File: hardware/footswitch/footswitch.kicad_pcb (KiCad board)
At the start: 2 copper layers, 34 x 24 mm, 4 parts, among them J1 Conn_02x05_Counter_Clockwise

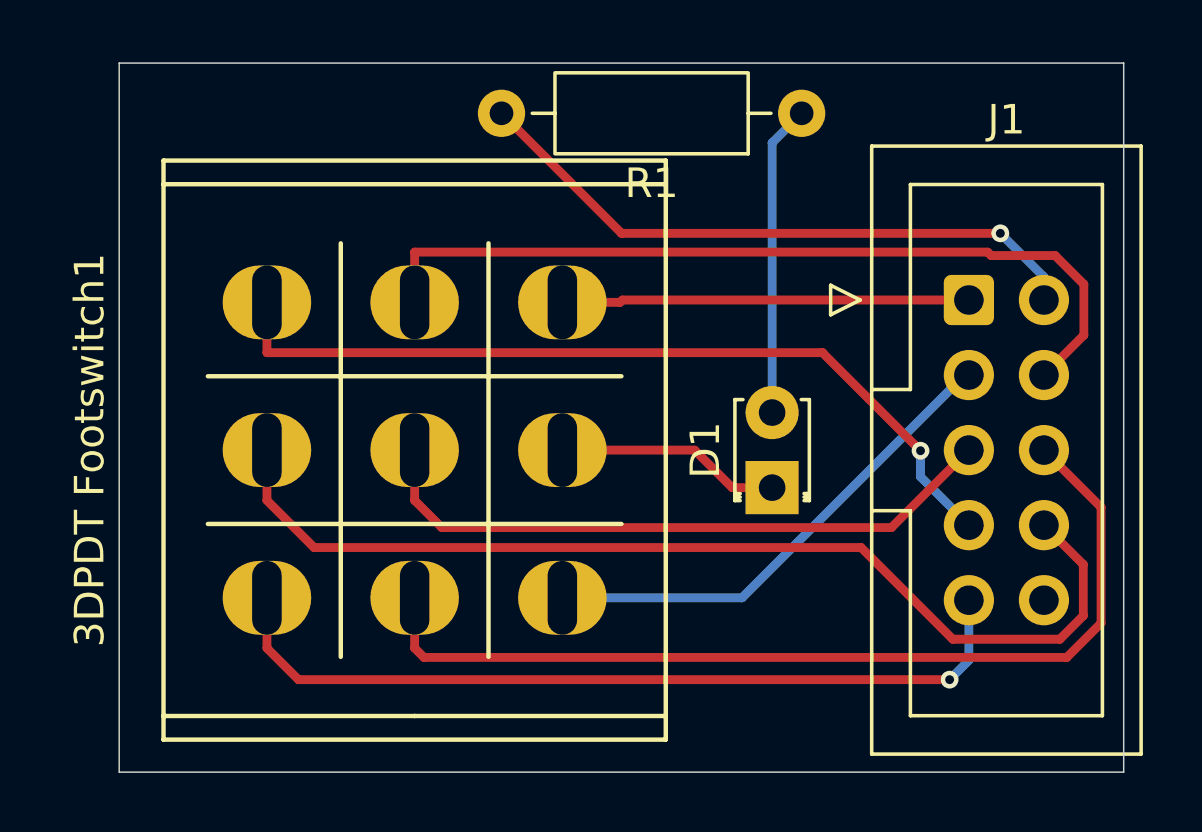
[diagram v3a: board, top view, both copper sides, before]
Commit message: Minor adjustments to footswitch pcb
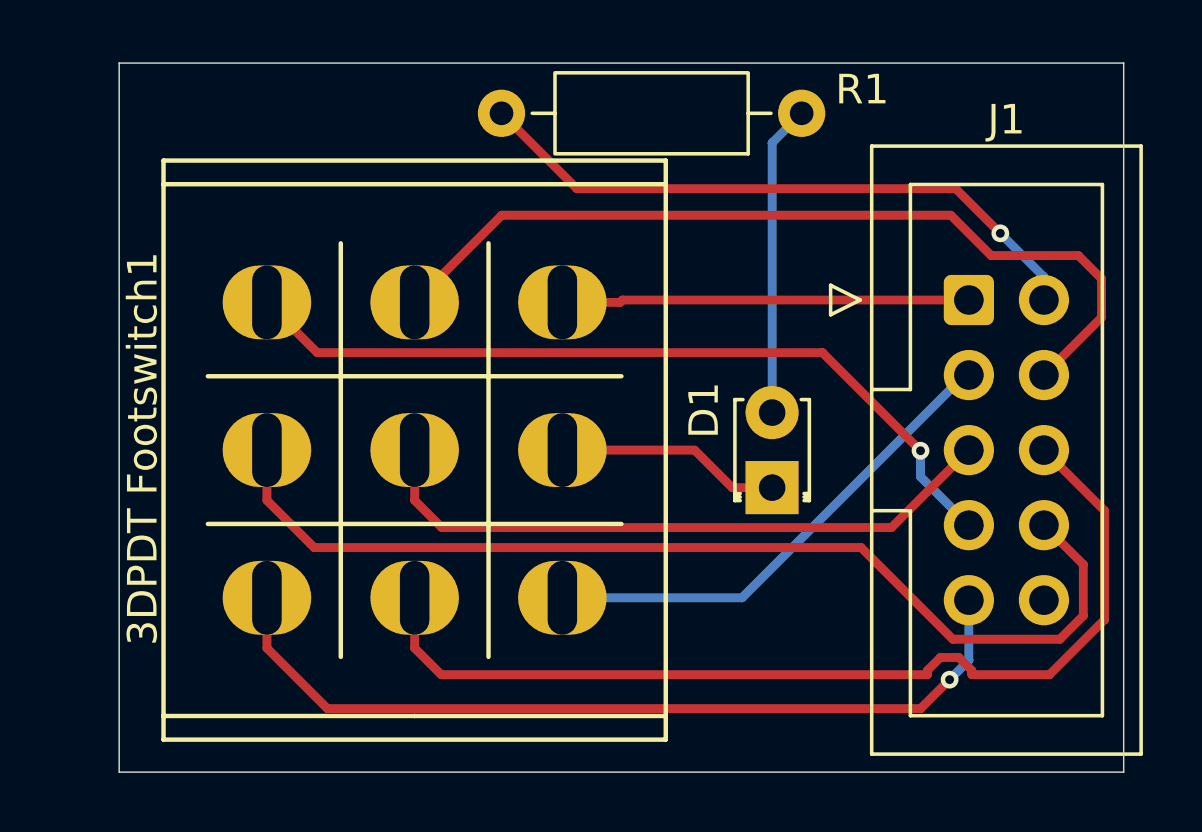
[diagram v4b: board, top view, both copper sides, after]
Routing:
- net /conn6: track 32.2 -> 33.4 mm
- net /conn7: track 28.4 -> 27.4 mm
- net /conn4: track 28.4 -> 29.4 mm
- net /conn9: track 28.2 -> 29.0 mm
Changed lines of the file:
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@@
 		(tags "Resistor Axial_DIN0207 series Axial Horizontal pin pitch 10.16mm 0.25W = 1/4W length 6.3mm diameter 2.5mm")
 		(property "Reference" "R1"
-			(at 5.08 -2.37 0)
+			(at -2.05 0.8 0)
 			(layer "F.SilkS")
 			(effects
@@
 		(tags "LED")
 		(property "Reference" "D1"
-			(at 1.27 -2.26 90)
+			(at 2.62 -2.3 90)
 			(layer "F.SilkS")
 			(effects
@@
 		(at 140 112.1 -90)
 		(property "Reference" "3DPDT Footswitch1"
-			(at 0 11 90)
+			(at -0.05 9.2 90)
 			(layer "F.SilkS")
 			(effects
@@
 	)
 	(segment
-		(start 135 117.1)
+		(start 135 118.8017)
+		(end 135 117.1)
+		(width 0.3)
+		(layer "F.Cu")
+		(net 2)
+	)
+	(segment
+		(start 158.1078 119.8694)
+		(end 157.1272 120.85)
+		(width 0.3)
+		(layer "F.Cu")
+		(net 2)
+	)
+	(segment
+		(start 137.0483 120.85)
 		(end 135 118.8017)
 		(width 0.3)
@@
 	)
 	(segment
-		(start 158.1078 119.8694)
-		(end 136.0677 119.8694)
-		(width 0.3)
-		(layer "F.Cu")
-		(net 2)
-	)
-	(segment
-		(start 136.0677 119.8694)
-		(end 135 118.8017)
+		(start 157.1272 120.85)
+		(end 137.0483 120.85)
 		(width 0.3)
 		(layer "F.Cu")
@@
 	)
 	(segment
-		(start 162.6515 106.4861)
-		(end 162.6515 108.2085)
+		(start 163.25 107.61)
+		(end 161.3 109.56)
 		(width 0.3)
 		(layer "F.Cu")
@@
 	)
 	(segment
-		(start 161.6801 105.5147)
-		(end 162.6515 106.4861)
+		(start 140 107.1)
+		(end 142.95 104.15)
 		(width 0.3)
 		(layer "F.Cu")
@@
 	(segment
 		(start 159.5137 105.5147)
-		(end 161.6801 105.5147)
+		(end 162.4647 105.5147)
 		(width 0.3)
 		(layer "F.Cu")
@@
 	)
 	(segment
-		(start 140 105.3983)
-		(end 159.3973 105.3983)
+		(start 163.25 106.3)
+		(end 163.25 107.61)
 		(width 0.3)
 		(layer "F.Cu")
@@
 	)
 	(segment
-		(start 162.6515 108.2085)
-		(end 161.3 109.56)
+		(start 162.4647 105.5147)
+		(end 163.25 106.3)
 		(width 0.3)
 		(layer "F.Cu")
@@
 	)
 	(segment
-		(start 140 107.1)
-		(end 140 105.3983)
+		(start 158.149 104.15)
+		(end 159.5137 105.5147)
 		(width 0.3)
 		(layer "F.Cu")
@@
 	)
 	(segment
-		(start 159.3973 105.3983)
-		(end 159.5137 105.5147)
+		(start 142.95 104.15)
+		(end 158.149 104.15)
 		(width 0.3)
 		(layer "F.Cu")
@@
 	)
 	(segment
-		(start 147.003 104.763)
+		(start 158.312 103.25)
+		(end 145.49 103.25)
+		(width 0.3)
+		(layer "F.Cu")
+		(net 4)
+	)
+	(segment
+		(start 145.49 103.25)
 		(end 142.94 100.7)
 		(width 0.3)
@@
 	(segment
 		(start 159.825 104.763)
-		(end 147.003 104.763)
+		(end 158.312 103.25)
 		(width 0.3)
 		(layer "F.Cu")
@@
 	)
 	(segment
+		(start 136.7017 108.8017)
+		(end 135 107.1)
+		(width 0.3)
+		(layer "F.Cu")
+		(net 5)
+	)
+	(segment
 		(start 153.8044 108.8017)
-		(end 135 108.8017)
+		(end 157.1234 112.1207)
 		(width 0.3)
 		(layer "F.Cu")
@@
 	)
 	(segment
-		(start 135 107.1)
-		(end 135 108.8017)
-		(width 0.3)
-		(layer "F.Cu")
-		(net 5)
-	)
-	(segment
-		(start 157.1234 112.1207)
-		(end 153.8044 108.8017)
+		(start 153.8044 108.8017)
+		(end 136.7017 108.8017)
 		(width 0.3)
 		(layer "F.Cu")
@@
 	)
 	(segment
-		(start 163.2344 117.9567)
-		(end 162.0734 119.1177)
+		(start 161.3 112.1)
+		(end 163.349 114.149)
 		(width 0.3)
 		(layer "F.Cu")
@@
 	)
 	(segment
-		(start 140 117.1)
+		(start 157.796725 119.1184)
+		(end 157.3568 119.558325)
+		(width 0.3)
+		(layer "F.Cu")
+		(net 7)
+	)
+	(segment
+		(start 157.3568 119.7)
+		(end 140.8983 119.7)
+		(width 0.3)
+		(layer "F.Cu")
+		(net 7)
+	)
+	(segment
+		(start 163.349 117.8421)
+		(end 161.4911 119.7)
+		(width 0.3)
+		(layer "F.Cu")
+		(net 7)
+	)
+	(segment
+		(start 157.3568 119.558325)
+		(end 157.3568 119.7)
+		(width 0.3)
+		(layer "F.Cu")
+		(net 7)
+	)
+	(segment
+		(start 140.8983 119.7)
 		(end 140 118.8017)
 		(width 0.3)
@@
 	)
 	(segment
-		(start 162.0734 119.1177)
-		(end 140.316 119.1177)
+		(start 161.4911 119.7)
+		(end 158.8588 119.7)
 		(width 0.3)
 		(layer "F.Cu")
@@
 	)
 	(segment
-		(start 163.2344 114.0344)
-		(end 163.2344 117.9567)
+		(start 140 118.8017)
+		(end 140 117.1)
 		(width 0.3)
 		(layer "F.Cu")
@@
 	)
 	(segment
-		(start 140.316 119.1177)
-		(end 140 118.8017)
+		(start 158.418875 119.1184)
+		(end 157.796725 119.1184)
 		(width 0.3)
 		(layer "F.Cu")
@@
 	)
 	(segment
-		(start 161.3 112.1)
-		(end 163.2344 114.0344)
-		(width 0.3)
-		(layer "F.Cu")
+		(start 158.8588 119.7)
+		(end 158.8588 119.558325)
+		(width 0.3)
+		(layer "F.Cu")
+		(net 7)
+	)
+	(segment
+		(start 158.8588 119.558325)
+		(end 158.418875 119.1184)
+		(width 0.3)
+		(layer "F.Cu")
+		(net 7)
+	)
+	(segment
+		(start 163.349 114.149)
+		(end 163.349 117.8421)
+		(width 0.3)
+		(layer "F.Cu")
